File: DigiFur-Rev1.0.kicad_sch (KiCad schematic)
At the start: 32 parts, among them SW1 SW_Push, SW2 SW_Push, SW3 SW_Push, SW4 SW_Push, SW5 SW_Push, U1 TLV840, U2 MCP23017x-x-SO, U3 NL17SZ10DBVT, U4 ESP32-C6-DevKitC-1, U5 RV-3032-C7, Y1 DSK321STD

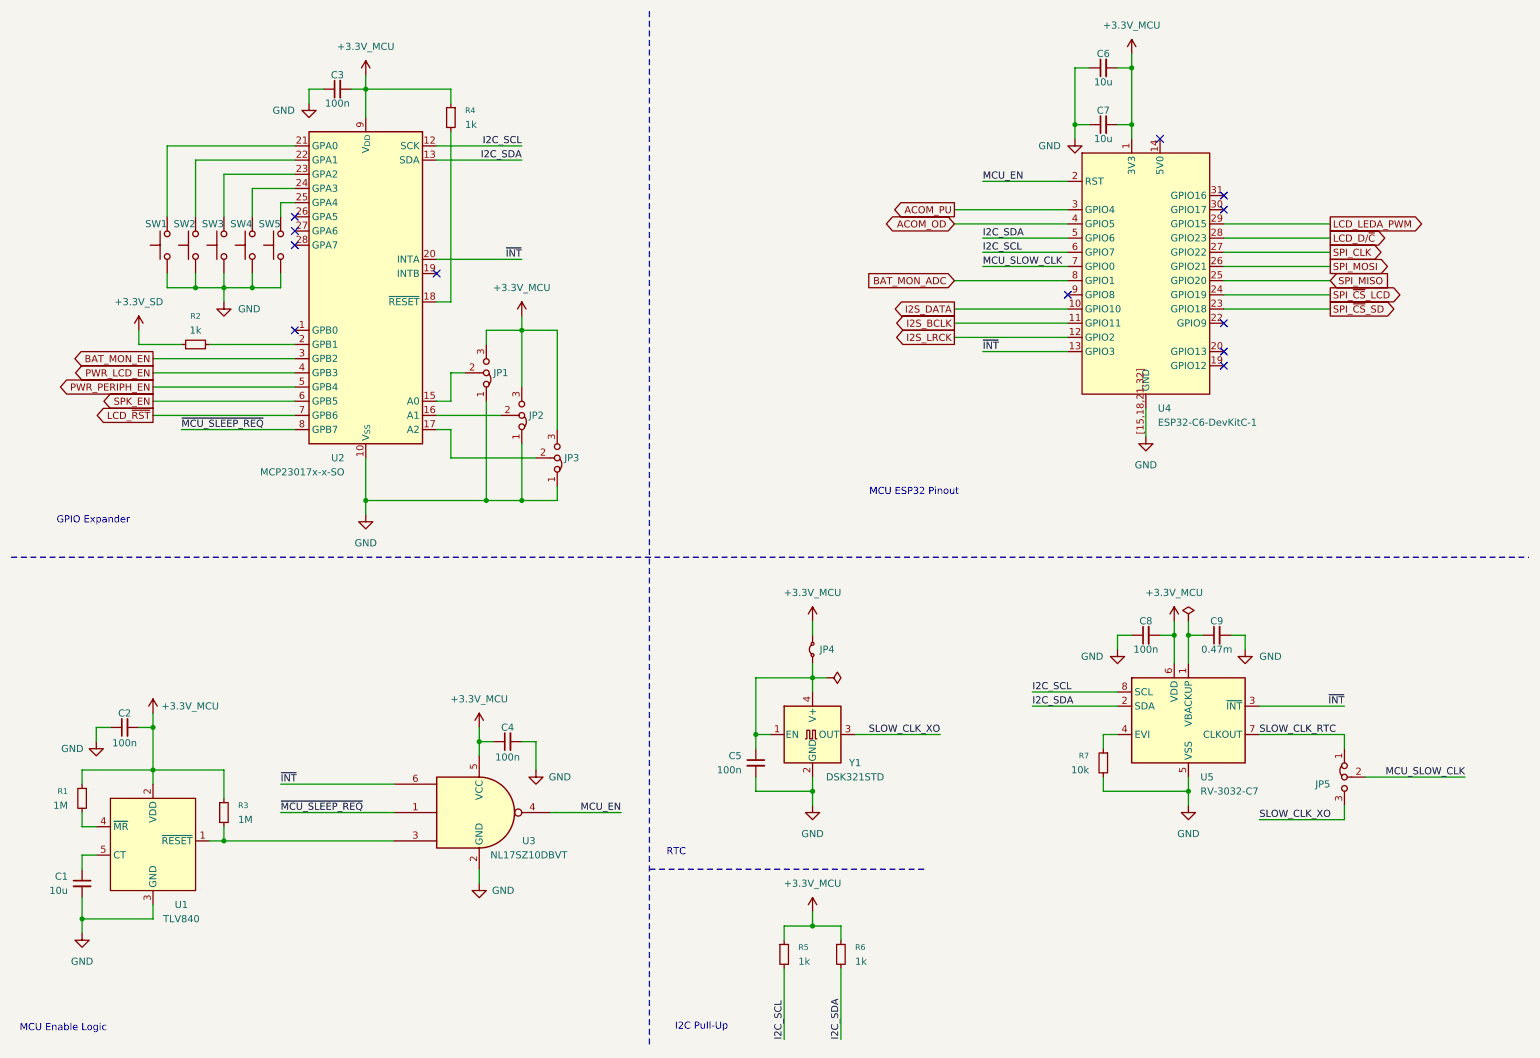
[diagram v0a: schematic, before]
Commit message: Initial layout before routing.
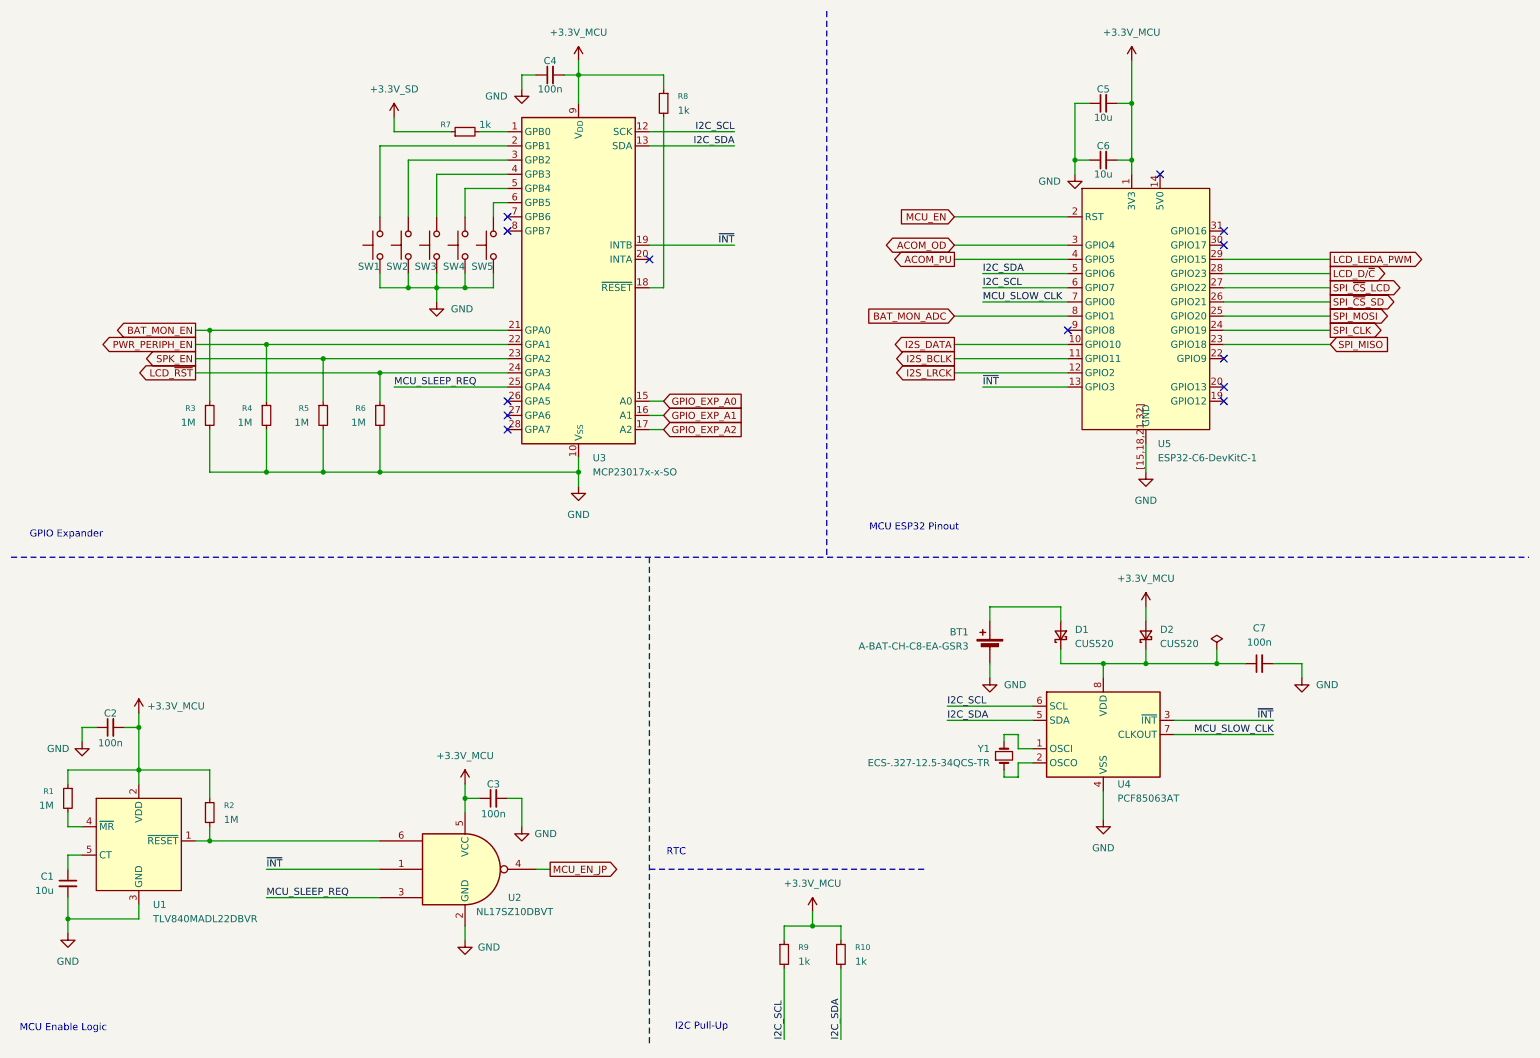
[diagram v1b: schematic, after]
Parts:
- removed C5, C8: 100n, Capacitor_SMD:C_0603_1608Metric_Pad1.08x0.95mm_HandSolder, symbol Device:C_Small
- removed C9: 0.47m, Capacitor_THT:CP_Radial_D13.0mm_P5.00mm, symbol Device:C_Small
- removed JP1, JP2, JP3: Jumper_3_Bridged12, Connector_PinHeader_2.54mm:PinHeader_1x03_P2.54mm_Vertical, symbol Jumper:Jumper_3_Bridged12
- removed JP4: Jumper_2_Small_Bridged, symbol Jumper:Jumper_2_Small_Bridged
- removed JP5: Jumper_3_Bridged12, symbol Jumper:Jumper_3_Bridged12
- removed R2: 1k, Resistor_SMD:R_0603_1608Metric_Pad0.98x0.95mm_HandSolder, symbol Device:R_Small
- removed U5: RV-3032-C7, Package_SON:MicroCrystal_C7_SON-8_1.5x3.2mm_P0.9mm, symbol project_symbols:RV-3032-C7
- removed Y1: DSK321STD, Oscillator:Oscillator_SMD_EuroQuartz_XO32-4Pin_3.2x2.5mm, symbol Oscillator:XO32
- added BT1: A-BAT-CH-C8-EA-GSR3, Battery:BatteryHolder_Keystone_1060_1x2032, symbol Device:Battery_Cell
- added C7: 100n, Capacitor_SMD:C_0603_1608Metric_Pad1.08x0.95mm_HandSolder, symbol Device:C_Small
- added D1, D2: CUS520, Diode_SMD:D_SOD-323_HandSoldering, symbol Device:D_Schottky_Small
- added R3, R4, R5, R6: 1M, Resistor_SMD:R_0603_1608Metric_Pad0.98x0.95mm_HandSolder, symbol Device:R_Small
- added U4: PCF85063AT, Package_SO:SOIC-8_3.9x4.9mm_P1.27mm, symbol project_symbols:PCF85063AT
- added Y1: ECS-.327-12.5-34QCS-TR, Crystal:Crystal_SMD_3215-2Pin_3.2x1.5mm, symbol Device:Crystal_Small
- R7: value 10k -> 1k
- SW1, SW2, SW3, SW4: footprint (none) -> Button_Switch_THT:SW_PUSH-12mm_Wuerth-430476085716
- SW5: value SW_Push -> MX2A-E1NW; footprint (none) -> Button_Switch_Keyboard:SW_Cherry_MX_1.00u_PCB
- U1: value TLV840 -> TLV840MADL22DBVR
- U5: renamed from U4; footprint project_footprints:ESP32-C6-DevKitC-1 -> project_footprints:ESP32-C6-DevKitC-Waveshare
- renumbered C4 to C3, C3 to C4, C6 to C5, C7 to C6, R6 to R10, R3 to R2, R4 to R8, R5 to R9, U3 to U2, U2 to U3
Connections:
- net +3.3V_MCU: now also D2.2 (A)
- net +3.3V_SD: now also R7.1
- net ACOM_OD: now also U5.3 (GPIO4); no longer U5.4 (GPIO5)
- net ACOM_PU: now also U5.4 (GPIO5); no longer U5.3 (GPIO4)
- net BAT_MON_EN: now also U3.21 (GPA0), R3.1; no longer U3.3 (GPB2)
- net GND: now also SW1.2, SW2.2, SW3.2, SW4.2, SW5.2, BT1.2 (-), C7.2, R3.2, R4.2, R5.2, R6.2, U4.4 (VSS); no longer R7.2, SW1.1, SW2.1, SW3.1, SW4.1, SW5.1
- net I2C_SCL: now also U4.6 (SCL)
- net I2C_SDA: now also U4.5 (SDA)
- net LCD_~{RST}: now also U3.24 (GPA3), R6.1; no longer U3.7 (GPB6)
- net MCU_EN: no longer U2.4
- net MCU_SLOW_CLK: now also U4.7 (CLKOUT)
- net PWR_PERIPH_EN: now also U3.22 (GPA1), R4.1; no longer U3.5 (GPB4)
- net SPI_CLK: now also U5.24 (GPIO19); no longer U5.27 (GPIO22)
- net SPI_MISO: now also U5.23 (GPIO18); no longer U5.25 (GPIO20)
- net SPI_MOSI: now also U5.25 (GPIO20); no longer U5.26 (GPIO21)
- net SPI_~{CS}_LCD: now also U5.27 (GPIO22); no longer U5.24 (GPIO19)
- net SPI_~{CS}_SD: now also U5.26 (GPIO21); no longer U5.23 (GPIO18)
- net SPK_EN: now also U3.23 (GPA2), R5.1; no longer U3.6 (GPB5)
- net ~{INT}: now also U2.1, U3.19 (INTB), U4.3 (~{INT}); no longer U2.6, U3.20 (INTA)
- net GPIO_EXP_A2: now reaches U3.17 (A2)
- net GPIO_EXP_A0: now reaches U3.15 (A0)
- net at R2.2, U1.1 (~{RESET}): now also U2.6; no longer U2.3
- net at U3.1 (GPB0): now also R7.2
- net GPIO_EXP_A1: now reaches U3.16 (A1)
- net at U3.2 (GPB1): now also SW1.1
- net MCU_SLEEP_REQ: now reaches U3.25 (GPA4)
- net MCU_SLEEP_REQ: now also U2.3; no longer SW5.2
- net PWR_LCD_EN: no longer names the net of U3.4 (GPB3)
- net PWR_LCD_EN: now also SW3.1
- net ~{MCU_SLEEP_REQ}: no longer names the net of U3.8 (GPB7)
- net ~{MCU_SLEEP_REQ}: no longer U2.1
- new net: BT1.1 (+), D1.2 (A)
- new net: SW2.1, U3.3 (GPB2)
- new net: SW4.1, U3.5 (GPB4)
- new net: SW5.1, U3.6 (GPB5)
- new net: C7.1, D1.1 (K), D2.1 (K), U4.8 (VDD)
- new net: U4.1 (OSCI), Y1.2
- new net: U4.2 (OSCO), Y1.1
- new net MCU_EN_JP: U2.4
- no-connect marks 12 -> 13
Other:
- moved on the sheet: C1, C2, C3, C4, C5, C6, R1, R2, R8, SW1, SW2, SW3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

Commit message: PCB layout done, signal routing finished, power routing remaining.
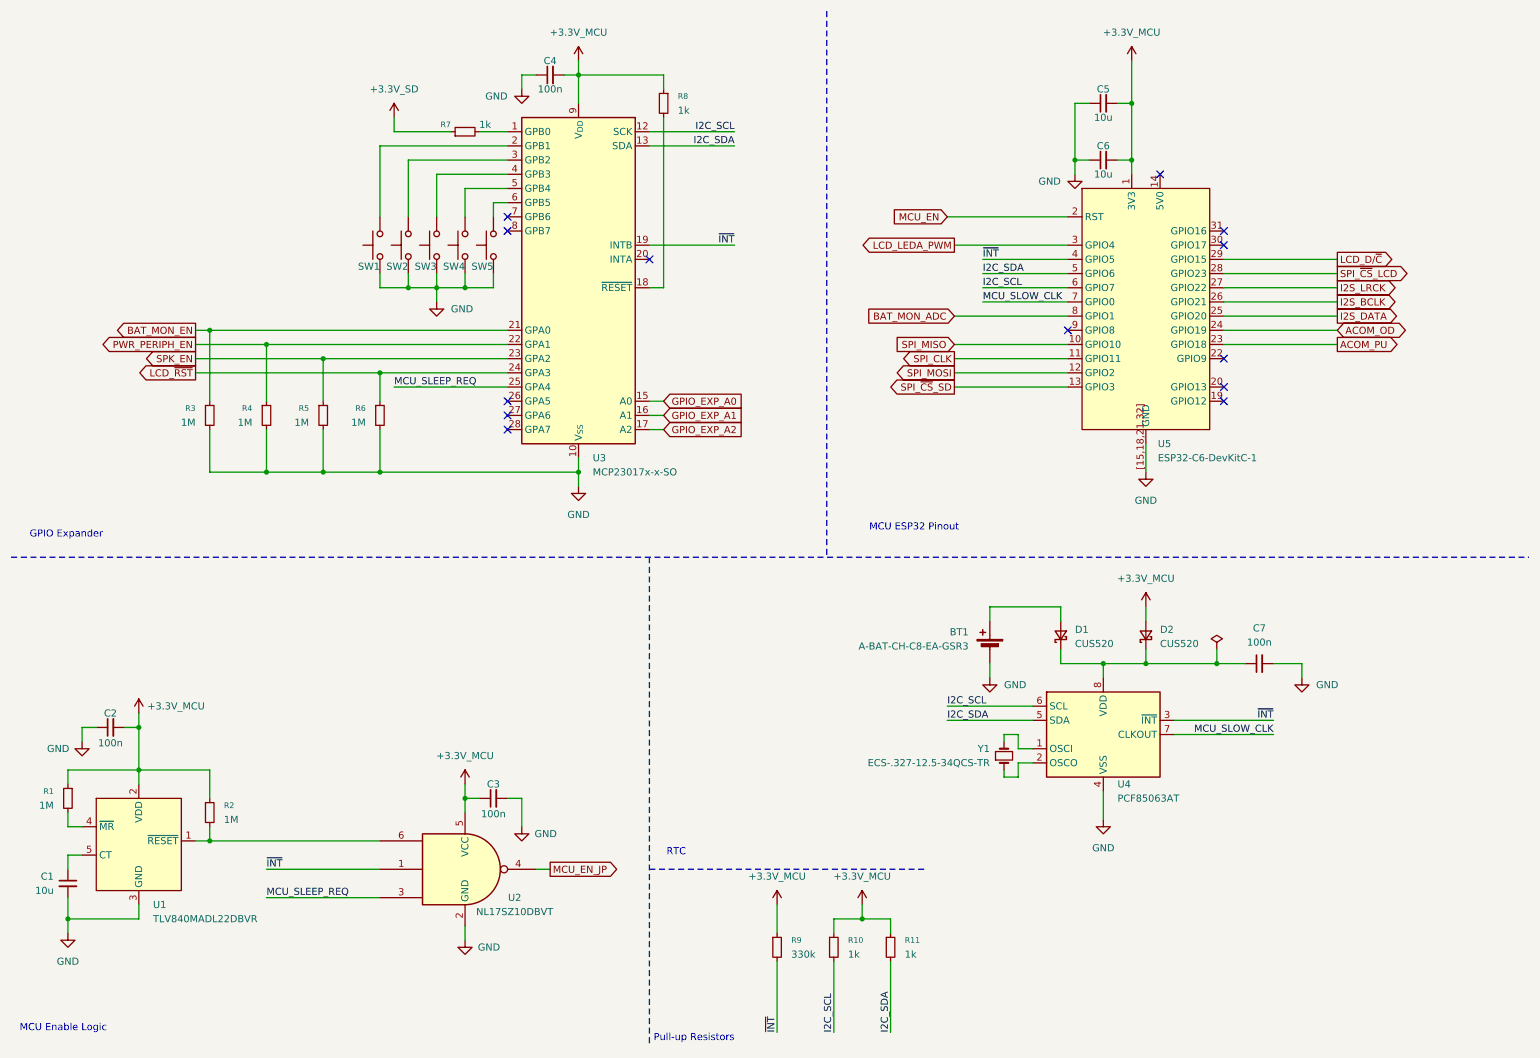
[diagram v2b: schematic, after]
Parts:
- added R9: 330k, Resistor_SMD:R_0603_1608Metric_Pad0.98x0.95mm_HandSolder, symbol Device:R_Small
- renumbered R9 to R10, R10 to R11
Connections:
- net +3.3V_MCU: now also R9.1
- net ACOM_OD: now also U5.24 (GPIO19); no longer U5.3 (GPIO4)
- net ACOM_PU: now also U5.23 (GPIO18); no longer U5.4 (GPIO5)
- net I2S_BCLK: now also U5.26 (GPIO21); no longer U5.11 (GPIO11)
- net I2S_DATA: now also U5.25 (GPIO20); no longer U5.10 (GPIO10)
- net I2S_LRCK: now also U5.27 (GPIO22); no longer U5.12 (GPIO2)
- net LCD_D/~{C}: now also U5.29 (GPIO15); no longer U5.28 (GPIO23)
- net LCD_LEDA_PWM: now also U5.3 (GPIO4); no longer U5.29 (GPIO15)
- net SPI_CLK: now also U5.11 (GPIO11); no longer U5.24 (GPIO19)
- net SPI_MISO: now also U5.10 (GPIO10); no longer U5.23 (GPIO18)
- net SPI_MOSI: now also U5.12 (GPIO2); no longer U5.25 (GPIO20)
- net SPI_~{CS}_LCD: now also U5.28 (GPIO23); no longer U5.27 (GPIO22)
- net SPI_~{CS}_SD: now also U5.13 (GPIO3); no longer U5.26 (GPIO21)
- net ~{INT}: now also U5.4 (GPIO5), R9.2; no longer U5.13 (GPIO3)
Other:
- note added: "Pull-up Resistors"
- note removed: "I2C Pull-Up"
- moved on the sheet: R10, R11
